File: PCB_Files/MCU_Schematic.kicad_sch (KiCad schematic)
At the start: 36 parts, among them J10 2D_LiDAR, J2 Ultrasonic_Sensor, J3 OLED_Display, J5 USB_C_Receptacle_USB2.0_16P, J6 SWD, J9 IMU, SW1 SW_SPDT, U1 STM32F411RETx, Y1 16MHz

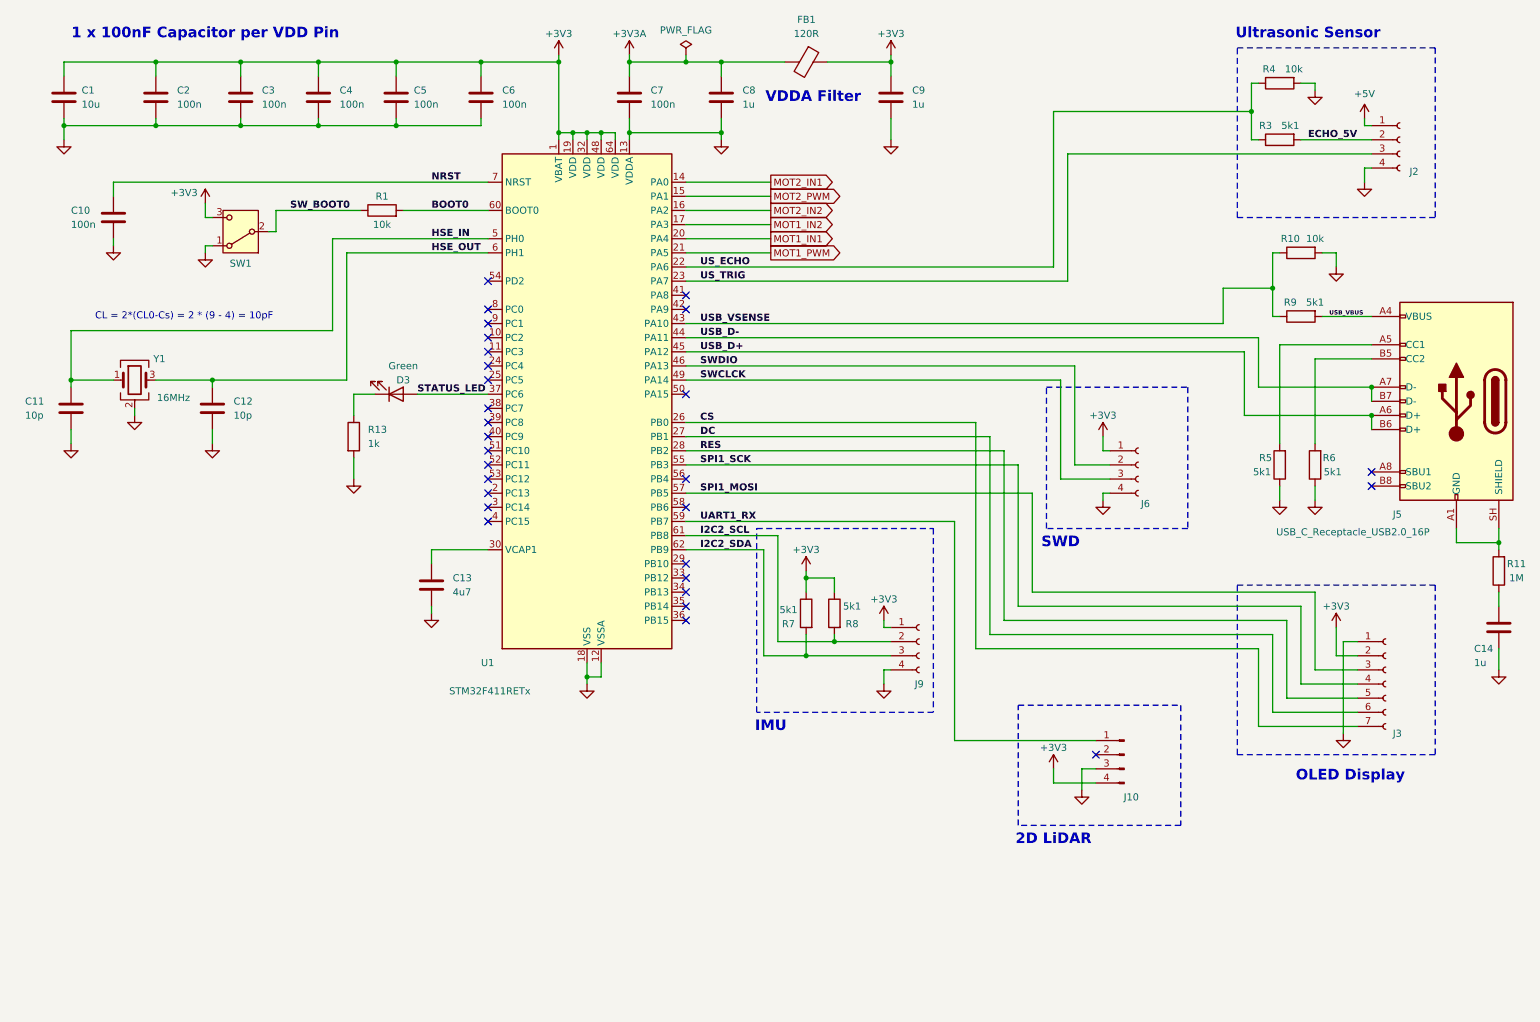
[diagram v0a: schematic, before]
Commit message: Cleaned up MCU schematic by removing speghetti wires and using local net labels instead (Only for some peripherals like sensors and USB.)
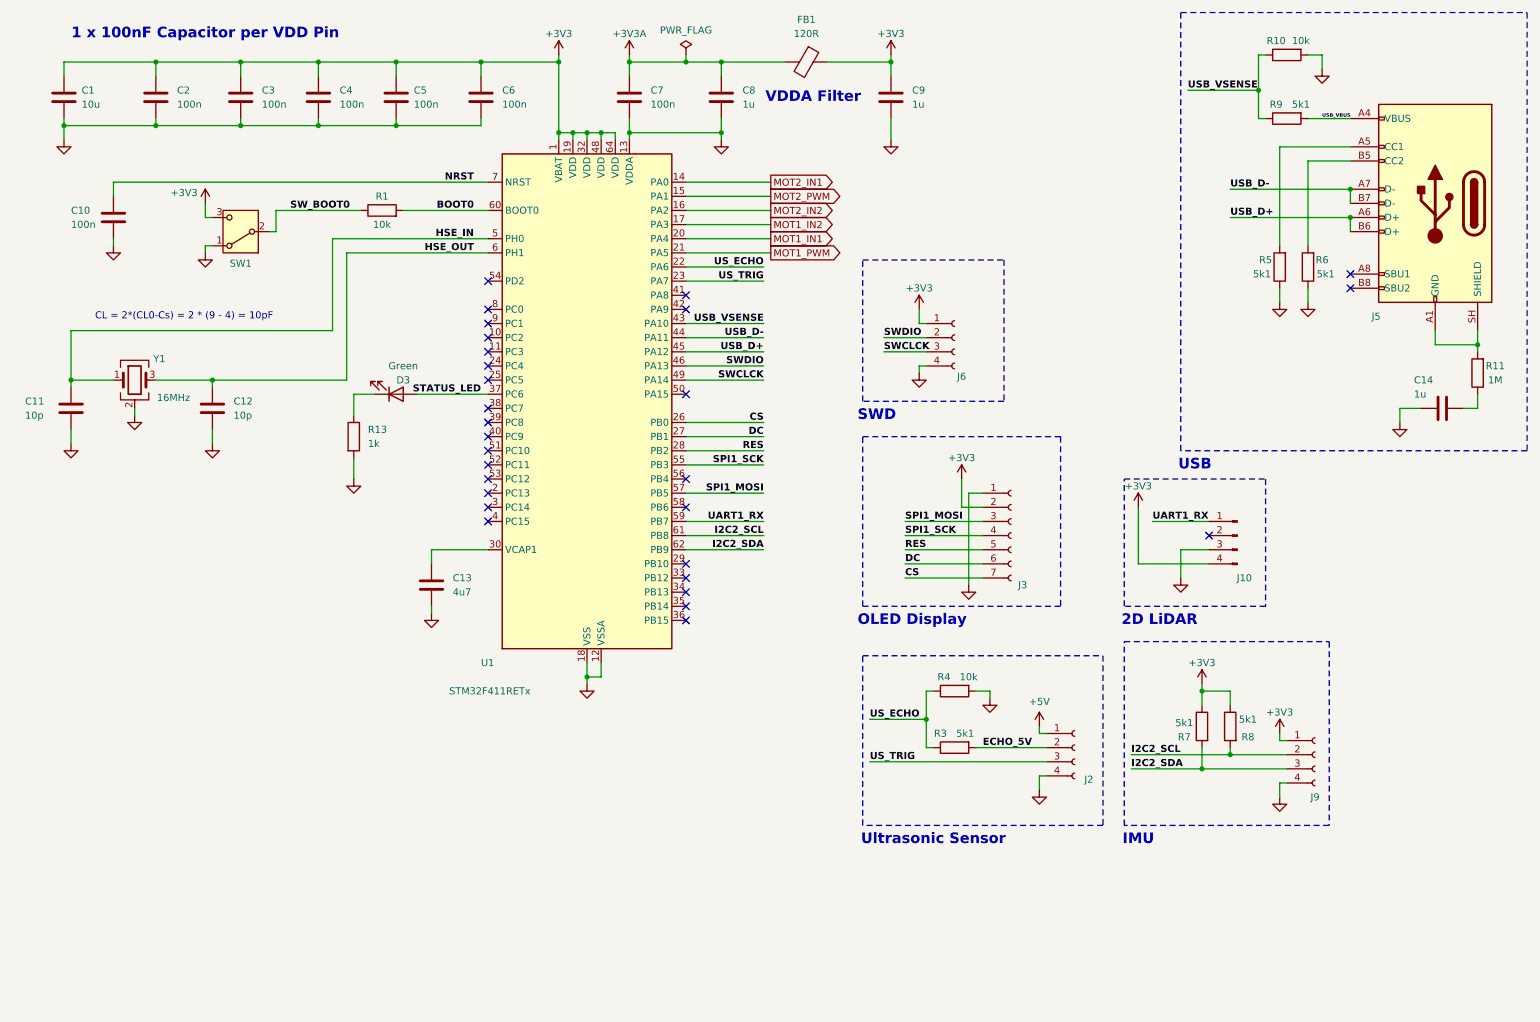
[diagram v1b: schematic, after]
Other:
- note added: "USB"
- moved on the sheet: C14, J10, J2, J3, J5, J6, J9, R10, R11, R3, R4, R5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

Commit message: Cleaned up MCU schematic by seperating power decoupling and main MCU. Added bounding boxes and labels to MCU power decoupling and the MCU itself.
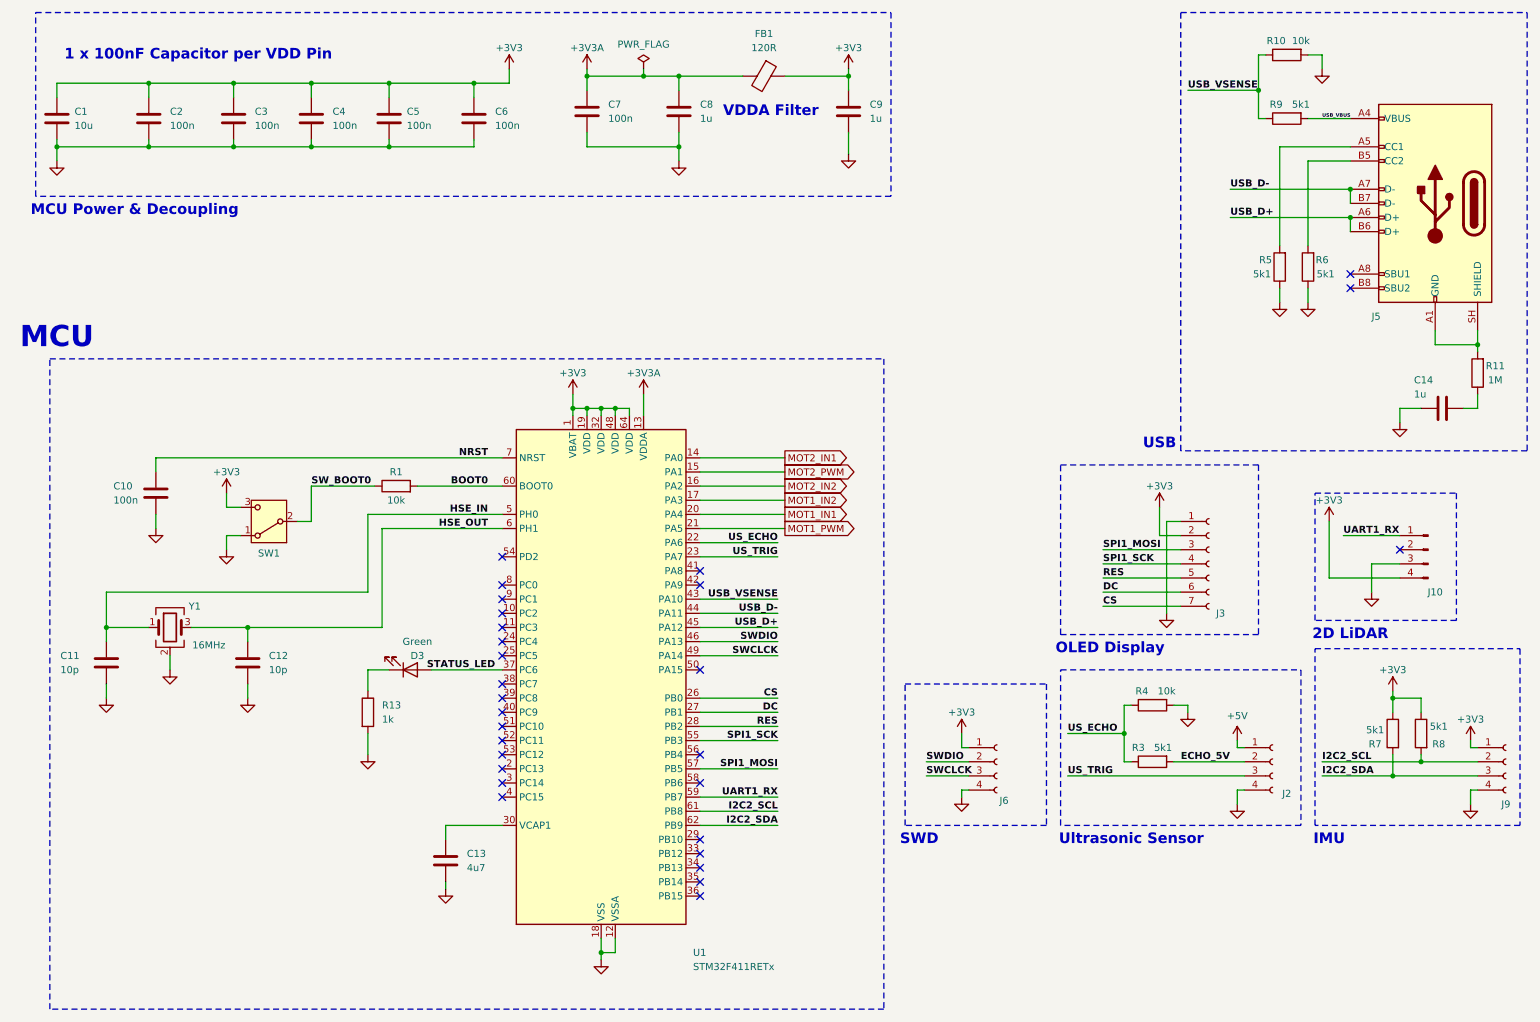
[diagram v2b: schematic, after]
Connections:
- net +3V3A: now also U1.13 (VDDA)
- net GND: no longer U1.13 (VDDA)
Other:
- note added: "MCU"
- note added: "MCU Power & Decoupling"
- note removed: "CL = 2*(CL0-Cs) = 2 * (9 - 4) = 10pF"
- moved on the sheet: C1, C10, C11, C12, C13, C2, C3, C4, C5, C6, C7, C8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

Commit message: Added DNP to IMU pull up resistors due to already being on the module.
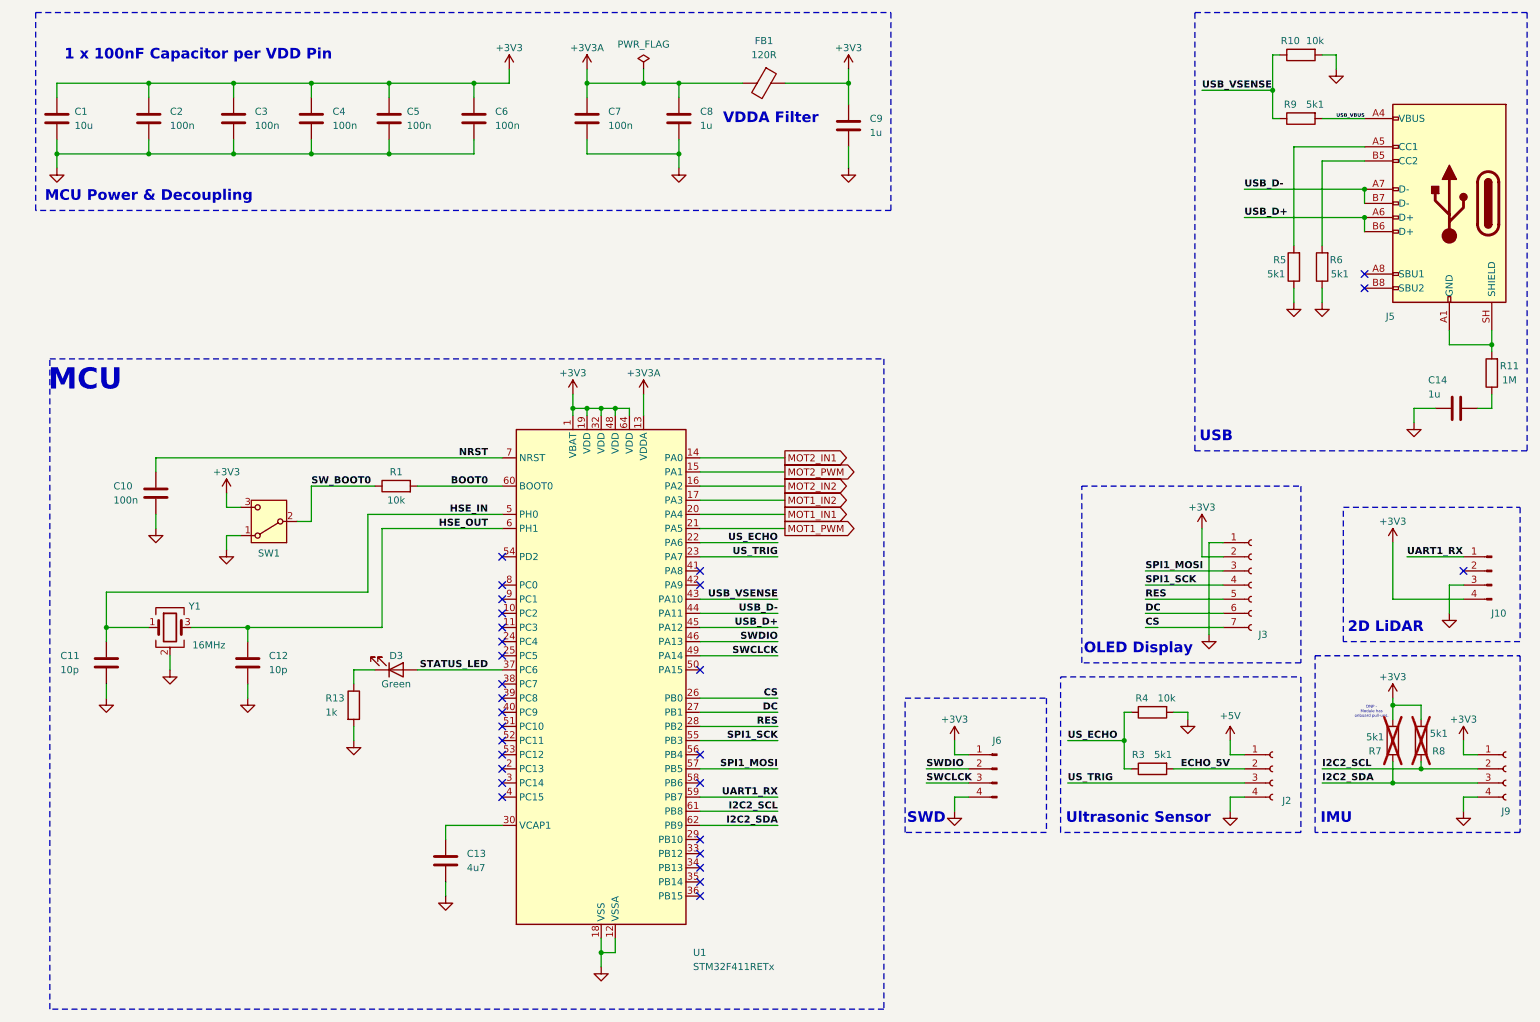
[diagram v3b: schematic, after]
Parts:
- J6: value SWD -> Conn_01x04_Pin; symbol Connector:Conn_01x04_Socket -> Connector:Conn_01x04_Pin
- R7, R8: now not fitted
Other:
- note added: "DNP - Module has onboard pull-ups."
- moved on the sheet: C14, C7, C8, C9, D3, FB1, J10, J2, J3, J5, J9, R10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
